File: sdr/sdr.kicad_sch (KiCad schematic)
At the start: 1 part

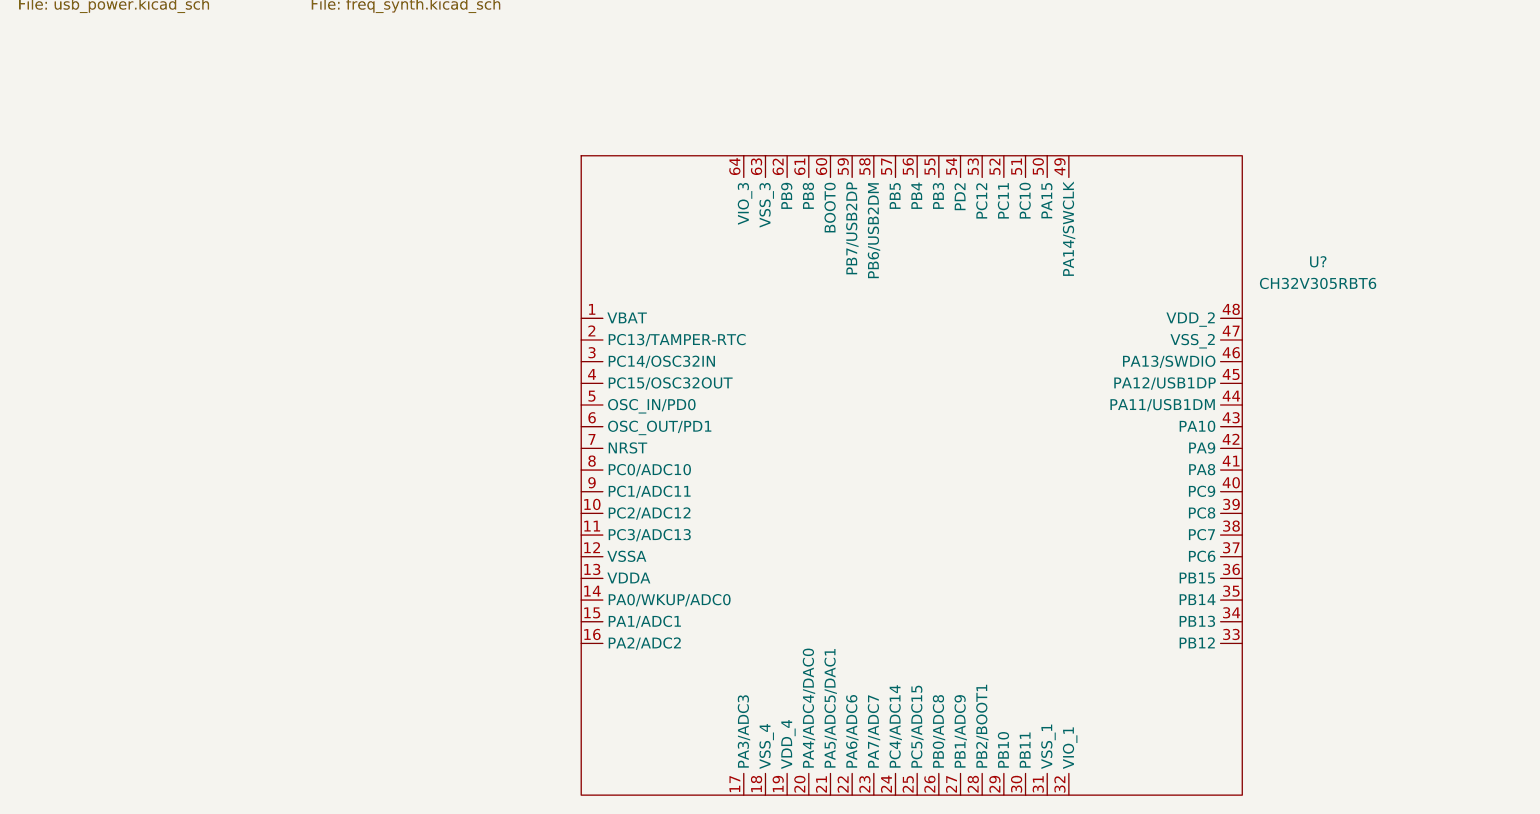
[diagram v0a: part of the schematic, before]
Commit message: Added 3.3V LDO and CPU sheet
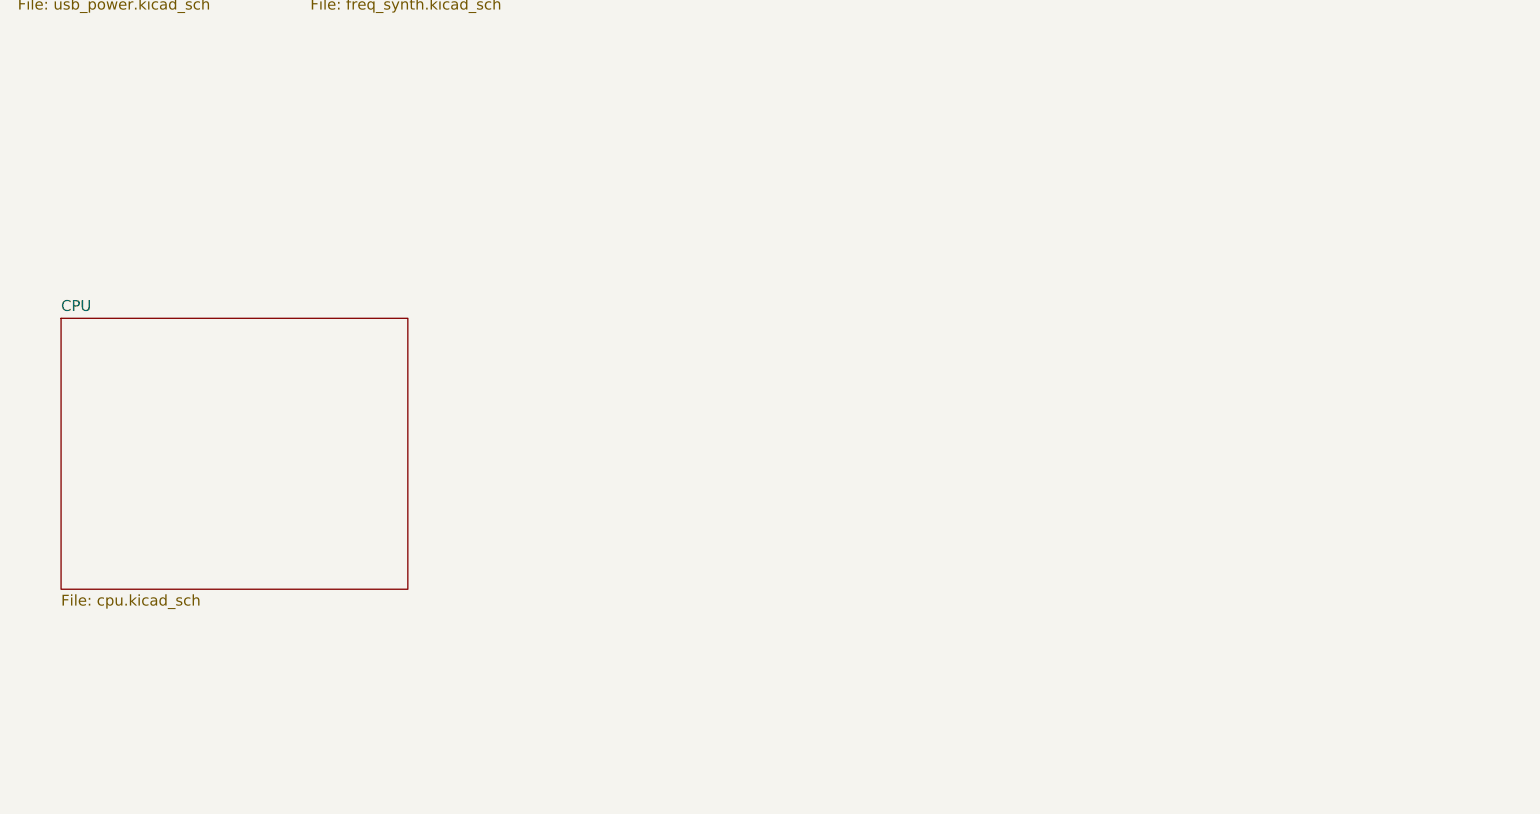
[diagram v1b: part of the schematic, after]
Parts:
- removed U?: CH32V305RBT6, symbol zl4aa:CH32V305RBT6
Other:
- added sheet CPU (cpu.kicad_sch)
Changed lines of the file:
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@@
 (kicad_sch (version 20211123) (generator eeschema)
   (paper "A4")
-  (symbol (lib_id "zl4aa:CH32V305RBT6") (at 148.59 116.84 0) (unit 1)
-    (in_bom yes) (on_board yes) (fields_autoplaced)
-    (property "Reference" "U?" (id 0) (at 196.85 91.2112 0))
-    (property "Value" "CH32V305RBT6" (id 1) (at 196.85 93.7512 0))
-    (property "Footprint" "" (id 2) (at 125.73 111.76 0)
-      (effects (font (size 1.27 1.27)) hide)
-    )
-    (property "Datasheet" "" (id 3) (at 125.73 111.76 0)
-      (effects (font (size 1.27 1.27)) hide)
-    )
-    (pin "1")
-    (pin "10")
-    (pin "11")
-    (pin "12")
-    (pin "13")
-    (pin "14")
-    (pin "15")
-    (pin "16")
-    (pin "17")
-    (pin "18")
-    (pin "19")
-    (pin "2")
-    (pin "20")
-    (pin "21")
-    (pin "22")
-    (pin "23")
-    (pin "24")
-    (pin "25")
-    (pin "26")
-    (pin "27")
-    (pin "28")
-    (pin "29")
-    (pin "3")
-    (pin "30")
-    (pin "31")
-    (pin "32")
-    (pin "33")
-    (pin "34")
-    (pin "35")
-    (pin "36")
-    (pin "37")
-    (pin "38")
-    (pin "39")
-    (pin "4")
-    (pin "40")
-    (pin "41")
-    (pin "42")
-    (pin "43")
-    (pin "44")
-    (pin "45")
-    (pin "46")
-    (pin "47")
-    (pin "48")
-    (pin "49")
-    (pin "5")
-    (pin "50")
-    (pin "51")
-    (pin "52")
-    (pin "53")
-    (pin "54")
-    (pin "55")
-    (pin "56")
-    (pin "57")
-    (pin "58")
-    (pin "59")
-    (pin "6")
-    (pin "60")
-    (pin "61")
-    (pin "62")
-    (pin "63")
-    (pin "64")
-    (pin "7")
-    (pin "8")
-    (pin "9")
-  )
   (sheet (at 44.45 40.64) (size 26.67 19.05) (fields_autoplaced)
     (stroke (width 0.1524) (type solid) (color 0 0 0 0))
@@
     (pin "AUDIO" input (at 237.49 53.34 180)
       (effects (font (size 1.27 1.27)) (justify left))
+    )
+  )
+  (sheet (at 49.53 97.79) (size 40.64 31.75) (fields_autoplaced)
+    (stroke (width 0.1524) (type solid) (color 0 0 0 0))
+    (fill (color 0 0 0 0.0000))
+    (property "Sheet name" "CPU" (id 0) (at 49.53 97.0784 0)
+      (effects (font (size 1.27 1.27)) (justify left bottom))
+    )
+    (property "Sheet file" "cpu.kicad_sch" (id 1) (at 49.53 130.1246 0)
+      (effects (font (size 1.27 1.27)) (justify left top))
     )
   )
@@
     (path "/f84f6323-5d0a-4b98-9173-b3e9afa6c9a5" (page "3"))
     (path "/54eba814-9a15-4896-a734-b24a06ae9330" (page "4"))
+    (path "/ad7b2242-3b39-40b3-b2e9-d6ea800dea9e" (page "5"))
   )
   (symbol_instances
@@
       (reference "#PWR014") (unit 1) (value "GND") (footprint "")
     )
+    (path "/236af311-fb12-40be-8aad-0a74644b9246/5f6ad648-aadd-4be7-b3c3-c6b948c4d7a6"
+      (reference "#PWR015") (unit 1) (value "+5V") (footprint "")
+    )
+    (path "/236af311-fb12-40be-8aad-0a74644b9246/7422161f-9447-4d18-bd9c-01050344d8f1"
+      (reference "#PWR016") (unit 1) (value "GND") (footprint "")
+    )
+    (path "/236af311-fb12-40be-8aad-0a74644b9246/d18cc4ba-c52d-4f3a-9ae4-1b407641a2e6"
+      (reference "#PWR017") (unit 1) (value "+3.3V") (footprint "")
+    )
+    (path "/ad7b2242-3b39-40b3-b2e9-d6ea800dea9e/f0576f5b-8d8a-409a-a2e5-d7901665c6a8"
+      (reference "#PWR018") (unit 1) (value "+3.3V") (footprint "")
+    )
+    (path "/ad7b2242-3b39-40b3-b2e9-d6ea800dea9e/1d093abc-361c-4140-b0bd-9d6ff0532576"
+      (reference "#PWR019") (unit 1) (value "GND") (footprint "")
+    )
+    (path "/ad7b2242-3b39-40b3-b2e9-d6ea800dea9e/4109361c-2078-40f7-bd4e-f49a2309c144"
+      (reference "#PWR020") (unit 1) (value "+3.3V") (footprint "")
+    )
+    (path "/ad7b2242-3b39-40b3-b2e9-d6ea800dea9e/92185aea-66c0-4684-bdde-08368ec64607"
+      (reference "#PWR021") (unit 1) (value "GND") (footprint "")
+    )
+    (path "/ad7b2242-3b39-40b3-b2e9-d6ea800dea9e/308a8678-069d-47c8-8005-c45598ff7791"
+      (reference "#PWR022") (unit 1) (value "+3.3V") (footprint "")
+    )
+    (path "/ad7b2242-3b39-40b3-b2e9-d6ea800dea9e/3cdd2840-f112-4f0d-adf6-2b6470eb6fc1"
+      (reference "#PWR023") (unit 1) (value "GND") (footprint "")
+    )
+    (path "/ad7b2242-3b39-40b3-b2e9-d6ea800dea9e/0250fec3-d614-45ed-af93-2d112774a209"
+      (reference "#PWR024") (unit 1) (value "+3.3V") (footprint "")
+    )
+    (path "/ad7b2242-3b39-40b3-b2e9-d6ea800dea9e/68cbc705-35e2-4065-95ff-f737f6bc303d"
+      (reference "#PWR025") (unit 1) (value "GND") (footprint "")
+    )
+    (path "/ad7b2242-3b39-40b3-b2e9-d6ea800dea9e/6ff4f4f9-1052-4ebd-8093-3644058ce124"
+      (reference "#PWR026") (unit 1) (value "+3.3V") (footprint "")
+    )
+    (path "/ad7b2242-3b39-40b3-b2e9-d6ea800dea9e/2410bd93-d037-4c91-bf42-d5060a7abfd1"
+      (reference "#PWR027") (unit 1) (value "GND") (footprint "")
+    )
     (path "/236af311-fb12-40be-8aad-0a74644b9246/e74075fc-3805-4d53-bde2-9873fa0e4668"
       (reference "C1") (unit 1) (value "10n") (footprint "Capacitor_SMD:C_0603_1608Metric")
@@
       (reference "C6") (unit 1) (value "1u") (footprint "Capacitor_SMD:C_0603_1608Metric")
     )
+    (path "/ad7b2242-3b39-40b3-b2e9-d6ea800dea9e/5abb69db-a15e-43c8-b374-a399ba4e6b8b"
+      (reference "C7") (unit 1) (value "10n") (footprint "")
+    )
+    (path "/ad7b2242-3b39-40b3-b2e9-d6ea800dea9e/c0e65267-a1a5-495f-ad56-afa8cbf9c1c1"
+      (reference "C8") (unit 1) (value "10n") (footprint "")
+    )
+    (path "/ad7b2242-3b39-40b3-b2e9-d6ea800dea9e/67cb7547-cf1e-4b96-9007-8ac39b4079fc"
+      (reference "C9") (unit 1) (value "10n") (footprint "")
+    )
+    (path "/ad7b2242-3b39-40b3-b2e9-d6ea800dea9e/11ff79c1-e535-4151-b66b-f2f34bc32f59"
+      (reference "C10") (unit 1) (value "10n") (footprint "")
+    )
+    (path "/ad7b2242-3b39-40b3-b2e9-d6ea800dea9e/7b7b32d8-00cf-48ea-b706-27965a329161"
+      (reference "C11") (unit 1) (value "10n") (footprint "")
+    )
     (path "/236af311-fb12-40be-8aad-0a74644b9246/7e509010-567b-4bf3-bfe1-bda6b202ba84"
       (reference "D1") (unit 1) (value "POWER") (footprint "Diode_SMD:D_0603_1608Metric")
@@
       (reference "U2") (unit 1) (value "LM4871M/TR_C383075") (footprint "Package_SO:SOP-8_3.9x4.9mm_P1.27mm")
     )
-    (path "/659b0967-f0df-484a-a429-77709fb0fa1f"
-      (reference "U?") (unit 1) (value "CH32V305RBT6") (footprint "")
+    (path "/236af311-fb12-40be-8aad-0a74644b9246/065d8083-db58-4bab-947e-edd6c3654893"
+      (reference "U3") (unit 1) (value "AMS1117-3.3") (footprint "Package_TO_SOT_SMD:SOT-223-3_TabPin2")
+    )
+    (path "/ad7b2242-3b39-40b3-b2e9-d6ea800dea9e/94c9ee2a-7b59-425f-a7cf-04c0e7a225e1"
+      (reference "U4") (unit 1) (value "CH32V305RBT6") (footprint "")
     )
     (path "/f84f6323-5d0a-4b98-9173-b3e9afa6c9a5/3fee64eb-3ef4-4c83-8d5f-ba65813cd0ca"

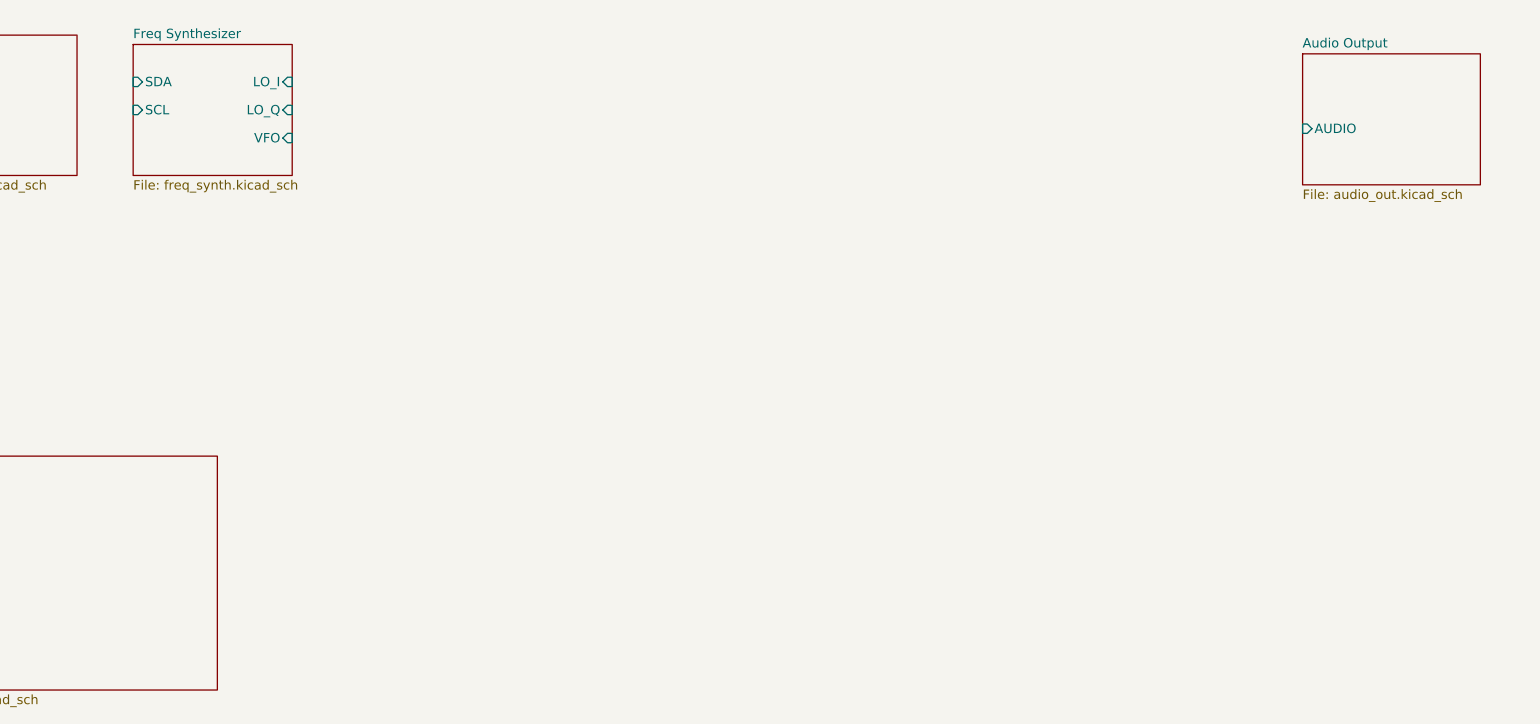
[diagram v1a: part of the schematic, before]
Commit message: Update lots of things. Now have basic CPU as well as some crude mixers
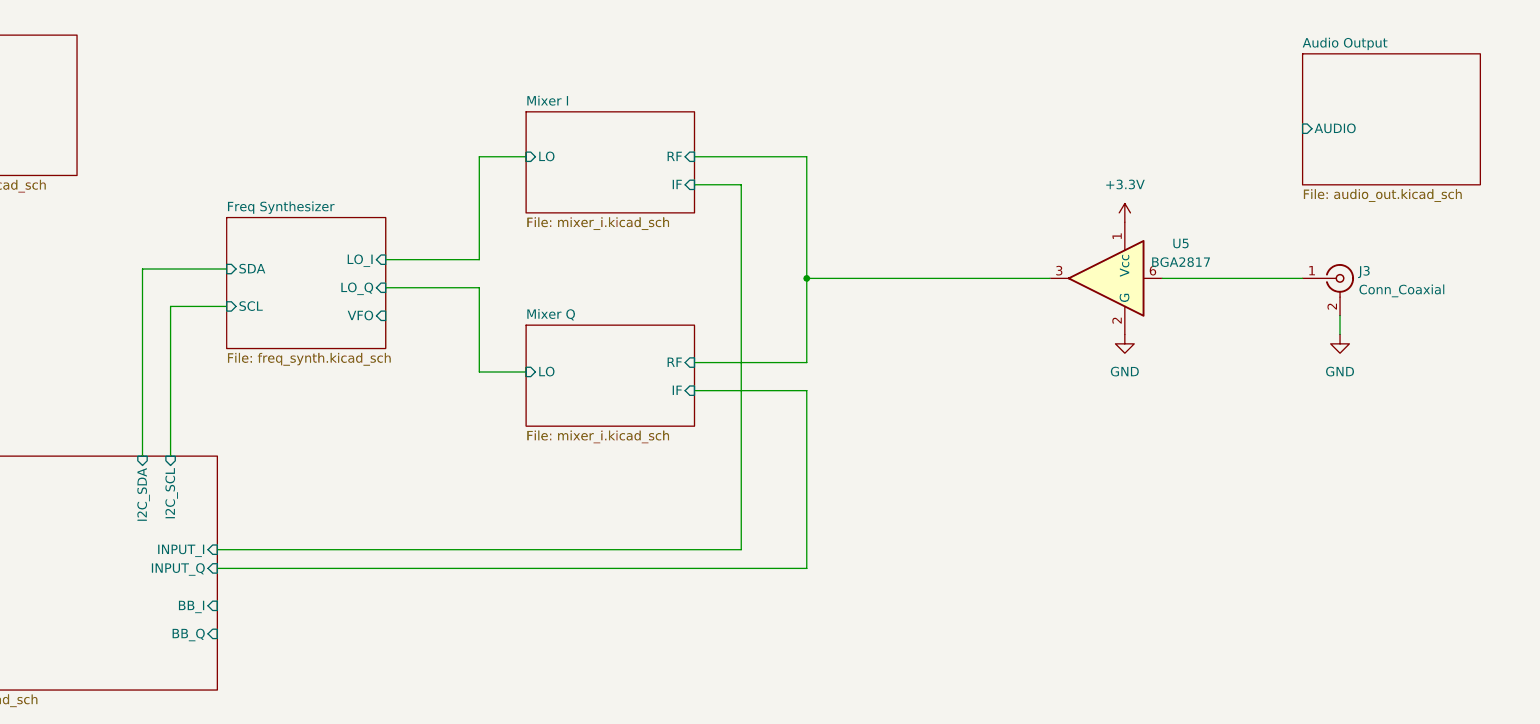
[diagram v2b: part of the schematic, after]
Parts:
- added J3: Conn_Coaxial, Connector_Coaxial:SMA_Amphenol_901-144_Vertical, symbol Connector:Conn_Coaxial
- added U5: BGA2817, Package_TO_SOT_SMD:SOT-363_SC-70-6, symbol RF_Amplifier:BGA2817
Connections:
- new net: J3.1 (In), U5.6
- new net +3.3V: U5.1 (Vcc)
- new net GND: J3.2 (Ext), U5.2 (G), U5.4 (G), U5.5 (G)
- new net Mixer I/RF: U5.3
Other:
- added sheet Mixer I (mixer_i.kicad_sch)
- added sheet Mixer Q (mixer_i.kicad_sch)
- sheet CPU ports: added BB_I, BB_Q, I2C_SCL, I2C_SDA, INPUT_I, INPUT_Q; removed none
